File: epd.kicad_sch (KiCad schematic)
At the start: 19 parts, among them J401 FH12A-24S-0.5SH(55), Q401 Q_NMOS_GSD

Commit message: Update to kicad 9
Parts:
- J401: value FH12A-24S-0.5SH(55) -> FH12A-24S-0.5SH(55)
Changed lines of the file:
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@@
 (kicad_sch
-	(version 20231120)
+	(version 20250114)
 	(generator "eeschema")
-	(generator_version "8.0")
+	(generator_version "9.0")
 	(paper "A4")
 	(junction
@@
 	(label "VDD"
 		(at 234.95 99.06 0)
-		(fields_autoplaced yes)
 		(effects
 			(font
@@
 	(label "VSH1"
 		(at 234.95 104.14 0)
-		(fields_autoplaced yes)
 		(effects
 			(font
@@
 	(label "RESE"
 		(at 88.9 92.71 0)
-		(fields_autoplaced yes)
 		(effects
 			(font
@@
 	(label "VSL"
 		(at 92.71 157.48 0)
-		(fields_autoplaced yes)
 		(effects
 			(font
@@
 	(label "VCOM"
 		(at 234.95 114.3 0)
-		(fields_autoplaced yes)
 		(effects
 			(font
@@
 	(label "SPI.~{CS}"
 		(at 201.93 83.82 0)
-		(fields_autoplaced yes)
 		(effects
 			(font
@@
 	(label "PREVGL"
 		(at 121.92 40.64 0)
-		(fields_autoplaced yes)
 		(effects
 			(font
@@
 	(label "PREVGL"
 		(at 234.95 111.76 0)
-		(fields_autoplaced yes)
 		(effects
 			(font
@@
 	(label "VPP"
 		(at 134.62 157.48 0)
-		(fields_autoplaced yes)
 		(effects
 			(font
@@
 	(label "VCOM"
 		(at 106.68 157.48 0)
-		(fields_autoplaced yes)
 		(effects
 			(font
@@
 	(label "VPP"
 		(at 234.95 101.6 0)
-		(fields_autoplaced yes)
 		(effects
 			(font
@@
 	(label "3V3"
 		(at 40.64 76.2 0)
-		(fields_autoplaced yes)
 		(effects
 			(font
@@
 	(label "PREVGH"
 		(at 234.95 106.68 0)
-		(fields_autoplaced yes)
 		(effects
 			(font
@@
 	(label "EPD_BUSY"
 		(at 234.95 76.2 0)
-		(fields_autoplaced yes)
 		(effects
 			(font
@@
 	(label "VSH2"
 		(at 234.95 66.04 0)
-		(fields_autoplaced yes)
 		(effects
 			(font
@@
 	(label "3V3"
 		(at 53.34 157.48 0)
-		(fields_autoplaced yes)
 		(effects
 			(font
@@
 	(label "EPD_RST"
 		(at 234.95 78.74 0)
-		(fields_autoplaced yes)
 		(effects
 			(font
@@
 	(label "VSH1"
 		(at 80.01 157.48 0)
-		(fields_autoplaced yes)
 		(effects
 			(font
@@
 	(label "EPD_D{slash}C"
 		(at 234.95 81.28 0)
-		(fields_autoplaced yes)
 		(effects
 			(font
@@
 	(label "PREVGH"
 		(at 113.03 76.2 0)
-		(fields_autoplaced yes)
 		(effects
 			(font
@@
 	(label "GDR"
 		(at 234.95 58.42 0)
-		(fields_autoplaced yes)
 		(effects
 			(font
@@
 	(label "RESE"
 		(at 234.95 60.96 0)
-		(fields_autoplaced yes)
 		(effects
 			(font
@@
 	(label "VSL"
 		(at 234.95 109.22 0)
-		(fields_autoplaced yes)
 		(effects
 			(font
@@
 	(label "VDD"
 		(at 120.65 157.48 0)
-		(fields_autoplaced yes)
 		(effects
 			(font
@@
 	(label "GDR"
 		(at 67.31 86.36 0)
-		(fields_autoplaced yes)
 		(effects
 			(font
@@
 	(label "3V3"
 		(at 234.95 91.44 180)
-		(fields_autoplaced yes)
 		(effects
 			(font
@@
 	(label "VSH2"
 		(at 66.04 157.48 0)
-		(fields_autoplaced yes)
 		(effects
 			(font
@@
 	(label "SPI.SCLK"
 		(at 201.93 86.36 0)
-		(fields_autoplaced yes)
 		(effects
 			(font
@@
 	(label "SPI.MOSI"
 		(at 201.93 88.9 0)
-		(fields_autoplaced yes)
 		(effects
 			(font
@@
 		(shape input)
 		(at 38.1 76.2 180)
-		(fields_autoplaced yes)
 		(effects
 			(font
@@
 		(shape input)
 		(at 227.33 81.28 180)
-		(fields_autoplaced yes)
 		(effects
 			(font
@@
 		(shape bidirectional)
 		(at 195.58 81.28 180)
-		(fields_autoplaced yes)
 		(effects
 			(font
@@
 		(shape input)
 		(at 227.33 78.74 180)
-		(fields_autoplaced yes)
 		(effects
 			(font
@@
 		(shape output)
 		(at 227.33 76.2 180)
-		(fields_autoplaced yes)
 		(effects
 			(font
@@
 			)
 		)
-		(property "Value" "FH12A-24S-0.5SH(55) "
+		(property "Value" "FH12A-24S-0.5SH(55)"
 			(at 257.81 52.07 0)
 			(effects

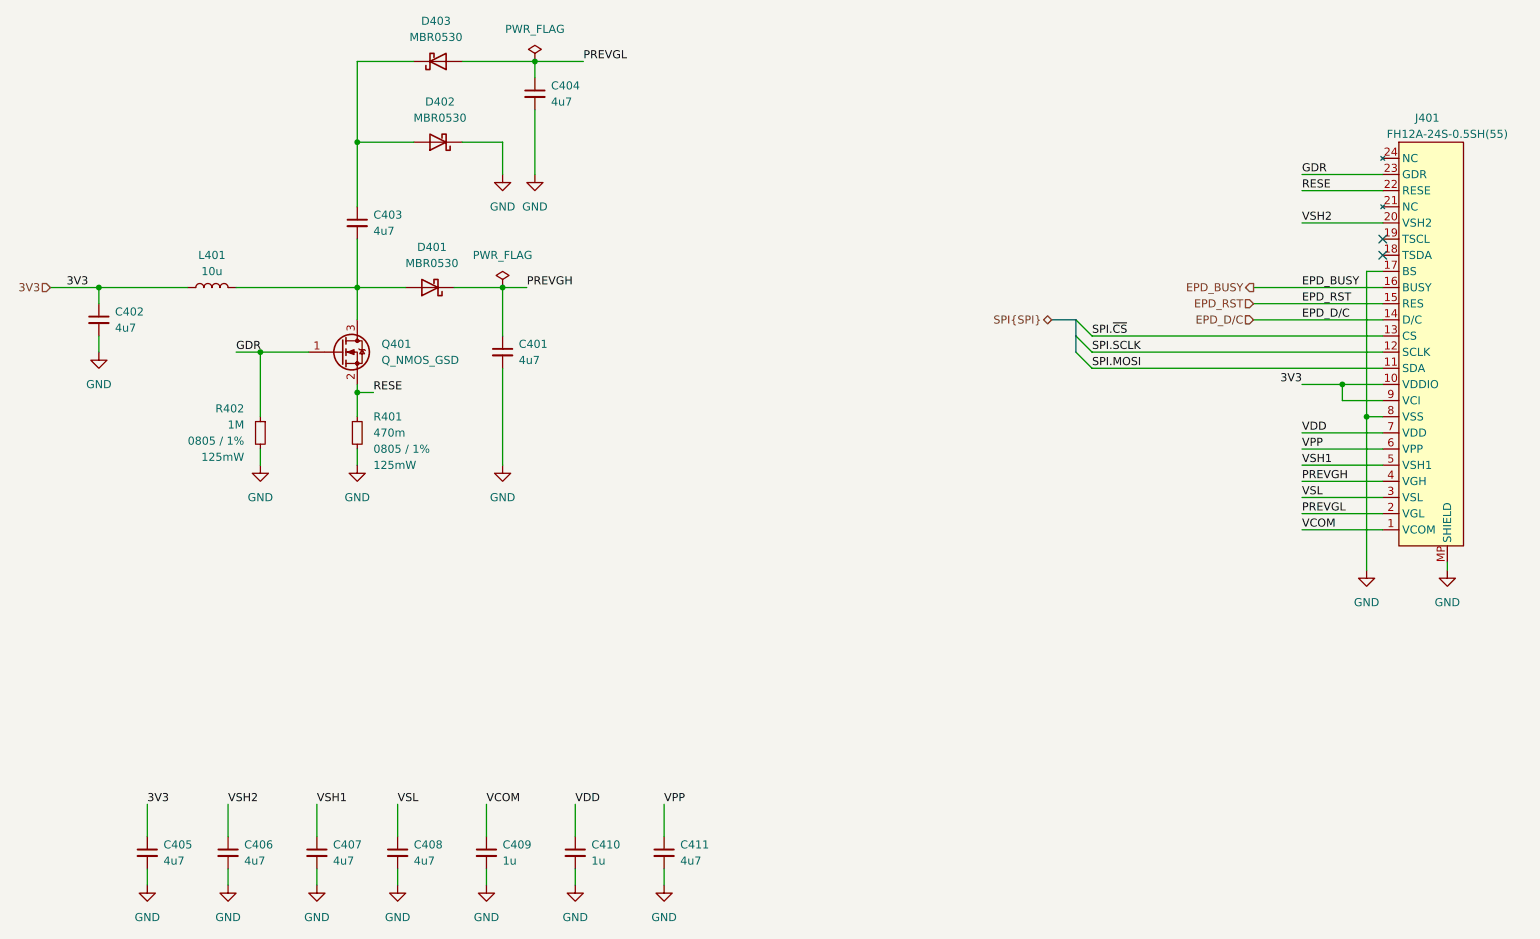
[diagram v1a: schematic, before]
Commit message: Update reference designators to single digit
Fits on the silk better
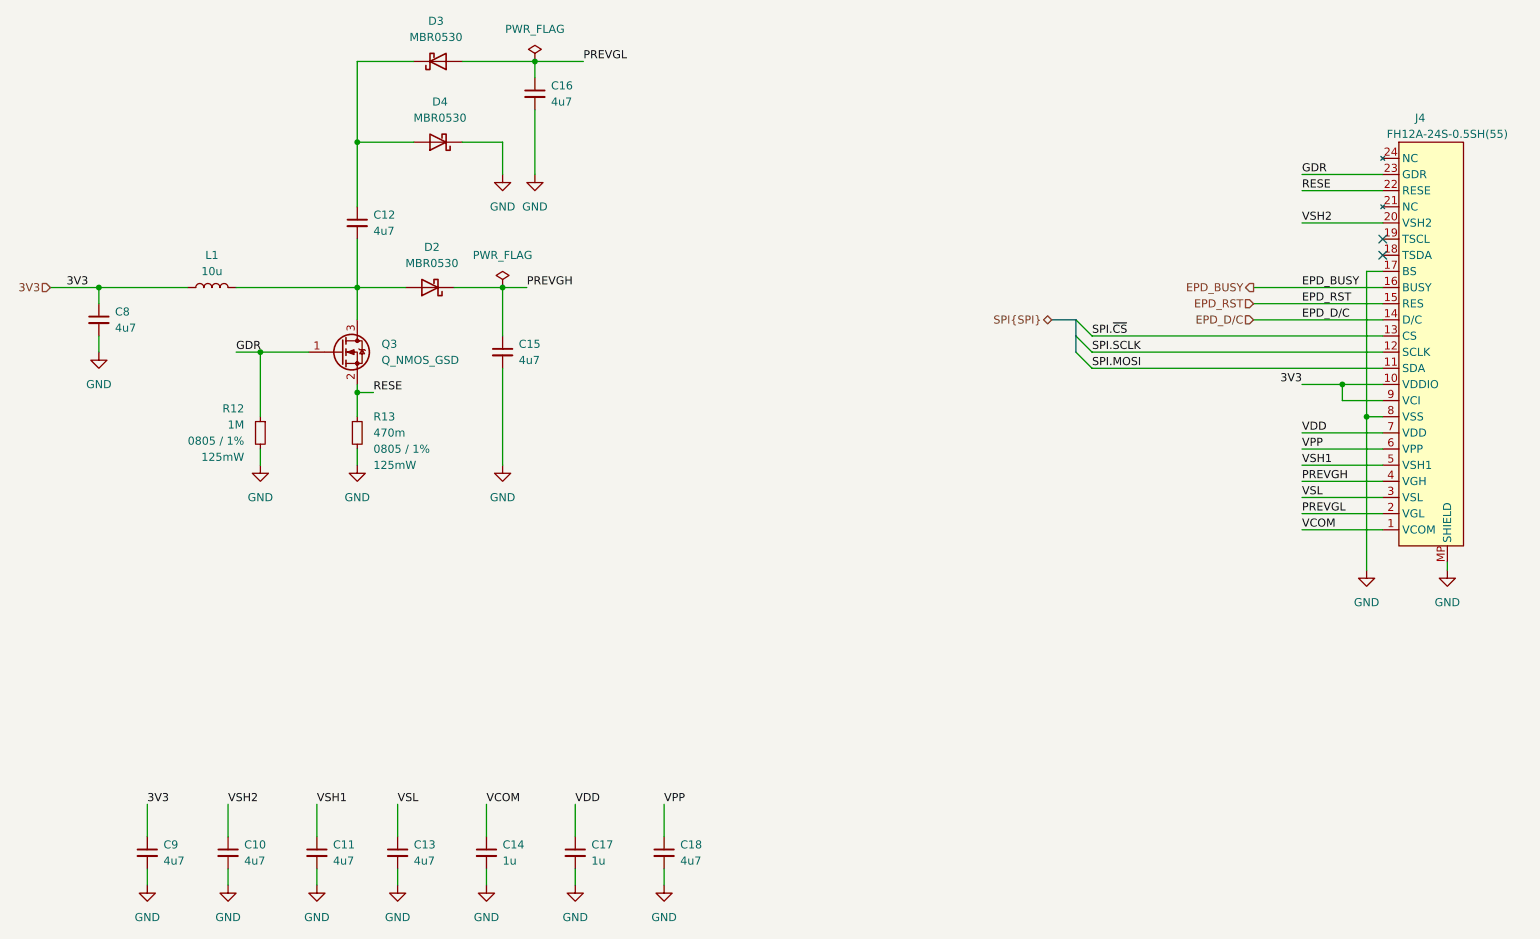
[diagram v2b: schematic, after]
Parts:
- renumbered C406 to C10, C407 to C11, C403 to C12, C408 to C13, C409 to C14, C401 to C15, C404 to C16, C410 to C17, C411 to C18, C402 to C8, C405 to C9, D401 to D2, D403 to D3, D402 to D4, J401 to J4, L401 to L1, Q401 to Q3, R402 to R12, R401 to R13

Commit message: Lighthouse
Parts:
- J4: symbol youdbetterrun:FPC24_Inverted -> bedroom_lights:FPC24_Inverted
- L1: footprint youdbetterrun:L_4x4x2.6 -> bedroom_lights:L_4x4x2.6
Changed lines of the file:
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@@
 		)
 		(instances
-			(project "youdbetterrun"
+			(project "bedroom_lights"
 				(path "/50da2b4e-34b1-4787-8ee6-5d7d17f804f4/d598949e-74c6-4803-8db9-612ef03f3111"
 					(reference "C15")
@@
 		)
 		(instances
-			(project "youdbetterrun"
+			(project "bedroom_lights"
 				(path "/50da2b4e-34b1-4787-8ee6-5d7d17f804f4/d598949e-74c6-4803-8db9-612ef03f3111"
 					(reference "#PWR018")
@@
 		)
 		(instances
-			(project "youdbetterrun"
+			(project "bedroom_lights"
 				(path "/50da2b4e-34b1-4787-8ee6-5d7d17f804f4/d598949e-74c6-4803-8db9-612ef03f3111"
 					(reference "#PWR030")
@@
 		)
 		(instances
-			(project "youdbetterrun"
+			(project "bedroom_lights"
 				(path "/50da2b4e-34b1-4787-8ee6-5d7d17f804f4/d598949e-74c6-4803-8db9-612ef03f3111"
 					(reference "#FLG05")
@@
 		)
 		(instances
-			(project "youdbetterrun"
+			(project "bedroom_lights"
 				(path "/50da2b4e-34b1-4787-8ee6-5d7d17f804f4/d598949e-74c6-4803-8db9-612ef03f3111"
 					(reference "C14")
@@
 		)
 		(instances
-			(project "youdbetterrun"
+			(project "bedroom_lights"
 				(path "/50da2b4e-34b1-4787-8ee6-5d7d17f804f4/d598949e-74c6-4803-8db9-612ef03f3111"
 					(reference "C8")
@@
 		)
 		(instances
-			(project "youdbetterrun"
+			(project "bedroom_lights"
 				(path "/50da2b4e-34b1-4787-8ee6-5d7d17f804f4/d598949e-74c6-4803-8db9-612ef03f3111"
 					(reference "#PWR027")
@@
 		)
 		(instances
-			(project "youdbetterrun"
+			(project "bedroom_lights"
 				(path "/50da2b4e-34b1-4787-8ee6-5d7d17f804f4/d598949e-74c6-4803-8db9-612ef03f3111"
 					(reference "#PWR020")
@@
 			)
 		)
-		(property "Footprint" "youdbetterrun:L_4x4x2.6"
+		(property "Footprint" "bedroom_lights:L_4x4x2.6"
 			(at 63.5 76.2 0)
 			(effects
@@
 		)
 		(instances
-			(project "youdbetterrun"
+			(project "bedroom_lights"
 				(path "/50da2b4e-34b1-4787-8ee6-5d7d17f804f4/d598949e-74c6-4803-8db9-612ef03f3111"
 					(reference "L1")
@@
 		)
 		(instances
-			(project "youdbetterrun"
+			(project "bedroom_lights"
 				(path "/50da2b4e-34b1-4787-8ee6-5d7d17f804f4/d598949e-74c6-4803-8db9-612ef03f3111"
 					(reference "D4")
@@
 		)
 		(instances
-			(project "youdbetterrun"
+			(project "bedroom_lights"
 				(path "/50da2b4e-34b1-4787-8ee6-5d7d17f804f4/d598949e-74c6-4803-8db9-612ef03f3111"
 					(reference "C13")
@@
 		)
 		(instances
-			(project "youdbetterrun"
+			(project "bedroom_lights"
 				(path "/50da2b4e-34b1-4787-8ee6-5d7d17f804f4/d598949e-74c6-4803-8db9-612ef03f3111"
 					(reference "D2")
@@
 		)
 		(instances
-			(project "youdbetterrun"
+			(project "bedroom_lights"
 				(path "/50da2b4e-34b1-4787-8ee6-5d7d17f804f4/d598949e-74c6-4803-8db9-612ef03f3111"
 					(reference "#PWR026")
@@
 		)
 		(instances
-			(project "youdbetterrun"
+			(project "bedroom_lights"
 				(path "/50da2b4e-34b1-4787-8ee6-5d7d17f804f4/d598949e-74c6-4803-8db9-612ef03f3111"
 					(reference "#PWR025")
@@
 		)
 		(instances
-			(project "youdbetterrun"
+			(project "bedroom_lights"
 				(path "/50da2b4e-34b1-4787-8ee6-5d7d17f804f4/d598949e-74c6-4803-8db9-612ef03f3111"
 					(reference "#PWR016")
@@
 		)
 		(instances
-			(project "youdbetterrun"
+			(project "bedroom_lights"
 				(path "/50da2b4e-34b1-4787-8ee6-5d7d17f804f4/d598949e-74c6-4803-8db9-612ef03f3111"
 					(reference "#PWR019")
@@
 		)
 		(instances
-			(project "youdbetterrun"
+			(project "bedroom_lights"
 				(path "/50da2b4e-34b1-4787-8ee6-5d7d17f804f4/d598949e-74c6-4803-8db9-612ef03f3111"
 					(reference "R13")
@@
 		)
 		(instances
-			(project "youdbetterrun"
+			(project "bedroom_lights"
 				(path "/50da2b4e-34b1-4787-8ee6-5d7d17f804f4/d598949e-74c6-4803-8db9-612ef03f3111"
 					(reference "C9")
@@
 		)
 		(instances
-			(project "youdbetterrun"
+			(project "bedroom_lights"
 				(path "/50da2b4e-34b1-4787-8ee6-5d7d17f804f4/d598949e-74c6-4803-8db9-612ef03f3111"
 					(reference "#PWR017")
@@
 		)
 		(instances
-			(project "youdbetterrun"
+			(project "bedroom_lights"
 				(path "/50da2b4e-34b1-4787-8ee6-5d7d17f804f4/d598949e-74c6-4803-8db9-612ef03f3111"
 					(reference "Q3")
@@
 		)
 		(instances
-			(project "youdbetterrun"
+			(project "bedroom_lights"
 				(path "/50da2b4e-34b1-4787-8ee6-5d7d17f804f4/d598949e-74c6-4803-8db9-612ef03f3111"
 					(reference "C16")
@@
 	)
 	(symbol
-		(lib_id "youdbetterrun:FPC24_Inverted")
+		(lib_id "bedroom_lights:FPC24_Inverted")
 		(at 255.27 85.09 0)
 		(unit 1)
@@
 		)
 		(instances
-			(project "youdbetterrun"
+			(project "bedroom_lights"
 				(path "/50da2b4e-34b1-4787-8ee6-5d7d17f804f4/d598949e-74c6-4803-8db9-612ef03f3111"
 					(reference "J4")
@@
 		)
 		(instances
-			(project "youdbetterrun"
+			(project "bedroom_lights"
 				(path "/50da2b4e-34b1-4787-8ee6-5d7d17f804f4/d598949e-74c6-4803-8db9-612ef03f3111"
 					(reference "#PWR029")
@@
 		)
 		(instances
-			(project "youdbetterrun"
+			(project "bedroom_lights"
 				(path "/50da2b4e-34b1-4787-8ee6-5d7d17f804f4/d598949e-74c6-4803-8db9-612ef03f3111"
 					(reference "C18")
@@
 		)
 		(instances
-			(project "youdbetterrun"
+			(project "bedroom_lights"
 				(path "/50da2b4e-34b1-4787-8ee6-5d7d17f804f4/d598949e-74c6-4803-8db9-612ef03f3111"
 					(reference "#FLG04")
@@
 		)
 		(instances
-			(project "youdbetterrun"
+			(project "bedroom_lights"
 				(path "/50da2b4e-34b1-4787-8ee6-5d7d17f804f4/d598949e-74c6-4803-8db9-612ef03f3111"
 					(reference "#PWR024")
@@
 		)
 		(instances
-			(project "youdbetterrun"
+			(project "bedroom_lights"
 				(path "/50da2b4e-34b1-4787-8ee6-5d7d17f804f4/d598949e-74c6-4803-8db9-612ef03f3111"
 					(reference "#PWR021")
@@
 		)
 		(instances
-			(project "youdbetterrun"
+			(project "bedroom_lights"
 				(path "/50da2b4e-34b1-4787-8ee6-5d7d17f804f4/d598949e-74c6-4803-8db9-612ef03f3111"
 					(reference "#PWR022")
@@
 		)
 		(instances
-			(project "youdbetterrun"
+			(project "bedroom_lights"
 				(path "/50da2b4e-34b1-4787-8ee6-5d7d17f804f4/d598949e-74c6-4803-8db9-612ef03f3111"
 					(reference "R12")
@@
 		)
 		(instances
-			(project "youdbetterrun"
+			(project "bedroom_lights"
 				(path "/50da2b4e-34b1-4787-8ee6-5d7d17f804f4/d598949e-74c6-4803-8db9-612ef03f3111"
 					(reference "#PWR028")
@@
 		)
 		(instances
-			(project "youdbetterrun"
+			(project "bedroom_lights"
 				(path "/50da2b4e-34b1-4787-8ee6-5d7d17f804f4/d598949e-74c6-4803-8db9-612ef03f3111"
 					(reference "D3")
@@
 		)
 		(instances
-			(project "youdbetterrun"
+			(project "bedroom_lights"
 				(path "/50da2b4e-34b1-4787-8ee6-5d7d17f804f4/d598949e-74c6-4803-8db9-612ef03f3111"
 					(reference "C12")
@@
 		)
 		(instances
-			(project "youdbetterrun"
+			(project "bedroom_lights"
 				(path "/50da2b4e-34b1-4787-8ee6-5d7d17f804f4/d598949e-74c6-4803-8db9-612ef03f3111"
 					(reference "C10")
@@
 		)
 		(instances
-			(project "youdbetterrun"
+			(project "bedroom_lights"
 				(path "/50da2b4e-34b1-4787-8ee6-5d7d17f804f4/d598949e-74c6-4803-8db9-612ef03f3111"
 					(reference "C17")
@@
 		)
 		(instances
-			(project "youdbetterrun"
+			(project "bedroom_lights"
 				(path "/50da2b4e-34b1-4787-8ee6-5d7d17f804f4/d598949e-74c6-4803-8db9-612ef03f3111"
 					(reference "C11")
@@
 		)
 		(instances
-			(project "youdbetterrun"
+			(project "bedroom_lights"
 				(path "/50da2b4e-34b1-4787-8ee6-5d7d17f804f4/d598949e-74c6-4803-8db9-612ef03f3111"
 					(reference "#PWR023")
